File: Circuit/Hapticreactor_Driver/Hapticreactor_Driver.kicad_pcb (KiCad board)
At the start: 2 copper layers, 24 parts, among them IC1 XCL103D503CR-G, J1 Conn_01x02, J2 Conn_01x02, J3 Conn_01x02, U1 XIAO ESP32C3, U2 TB6552FNG_C_8_EL, U3 MCP4725xxx-xCH

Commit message: ハプティックリアクタ用基板完成
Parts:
- removed C2: 0.1u, Capacitor_SMD:C_0603_1608Metric_Pad1.08x0.95mm_HandSolder
- removed C3, C4: 10u, Capacitor_SMD:C_1206_3216Metric_Pad1.33x1.80mm_HandSolder
- removed IC1: XCL103D503CR-G, User:XCL103D503CRG
- removed R7: 10k, Resistor_SMD:R_0603_1608Metric_Pad0.98x0.95mm_HandSolder
- added H4: MountingHole, MountingHole:MountingHole_2.2mm_M2, F.Cu at (142.6, 70.4)
- C1, JP1, R1, R2, R3, R4, R5, U2, U3: moved to B.Cu
- C5: value C -> 0.1u; moved to B.Cu
- R6: value R -> 1k; moved to B.Cu
- moved R2 36.2 mm to (126.2, 72.3), turned to -90 degrees
- moved R1 36.2 mm to (124.6, 72.3), turned to 90 degrees
- moved J3 34.8 mm to (117.2, 77.0), turned to -90 degrees
- moved H1 32.7 mm to (116.4, 70.4)
- moved J2 32.5 mm to (141.6, 76.8), turned to 90 degrees
- moved H2 28.0 mm to (116.4, 84.4)
- moved C1 27.1 mm to (134.4, 71.0), turned to 90 degrees
- moved J1 24.4 mm to (141.6, 80.4), turned to 90 degrees
- moved U3 24.0 mm to (129.3, 83.1), turned to -90 degrees
- moved R3 23.1 mm to (133.2, 84.6)
- moved C5 22.6 mm to (132.5, 78.6)
- moved R6 20.6 mm to (125.6, 85.2)
- moved U2 19.8 mm to (130.4, 73.0), turned to 90 degrees
- moved H3 19.7 mm to (142.6, 84.4)
- moved JP1 18.3 mm to (132.6, 81.9), turned to 90 degrees
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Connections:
- R6 pad 1: /XIAO_ESP32_C3/D7/GPIO20 -> /XIAO_ESP32_C3/D6/GPIO6
- U2 pad 6: +5V -> +3.3V
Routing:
- net Net-(D1-A): track 0.00 -> 24.6 mm, vias 0 -> 1
- net /Motor_Driver/B_OUT_2: track 0.00 -> 20.4 mm
- net /Motor_Driver/B_OUT_1: track 0.00 -> 17.8 mm
- net +3.3V: track 0.00 -> 17.6 mm, vias 0 -> 3
- net /Motor_Driver/A_OUT_2: track 0.00 -> 17.4 mm, vias 0 -> 2
- net /DAC/DAC_OUT: track 0.00 -> 17.3 mm
- net /Motor_Driver/PWM_IN_B2: track 0.00 -> 17.3 mm, vias 0 -> 1
- net /Motor_Driver/A_OUT_1: track 0.00 -> 15.4 mm, vias 0 -> 2
- net /DAC/DAC_SDA: track 0.00 -> 14.9 mm, vias 0 -> 2
- net /Motor_Driver/PWM_IN_A2: track 0.00 -> 13.9 mm, vias 0 -> 1
- net /DAC/DAC_SCL: track 0.00 -> 13.7 mm, vias 0 -> 2
- net /XIAO_ESP32_C3/BATT_IN+: track 0.00 -> 13.6 mm
- net /Motor_Driver/PWM_IN_A1: track 0.00 -> 13.6 mm, vias 0 -> 1
- net /XIAO_ESP32_C3/BATT_IN-: track 0.00 -> 10.5 mm
- net /Motor_Driver/PWM_IN_B1: track 0.00 -> 9.48 mm, vias 0 -> 1
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- added copper zone on B.Cu, net +3.3V
- added copper zone on B.Cu, net GND
- added copper zone on F.Cu, net GND
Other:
- board outline added: 31 x 18.8 mm
- board text added: "A1 A2"
- board text added: "B1 B2"
- board text added: "D1/A1"
- board text added: "D2,D3"
- board text added: "D4"
- board text added: "D5"
- board text added: "D6"
- board text added: "D7,D10"
- board text added: "DAC"
- board text added: "I2C_Address 0x60 0x61"
- board text added: "Li-ion 3.7V"
- board text added: "Li-ion Vol"
- board text added: "PWM_A"
- board text added: "PWM_B"
- board text added: "SCL"
- board text added: "SDA"
- board text added: "→"

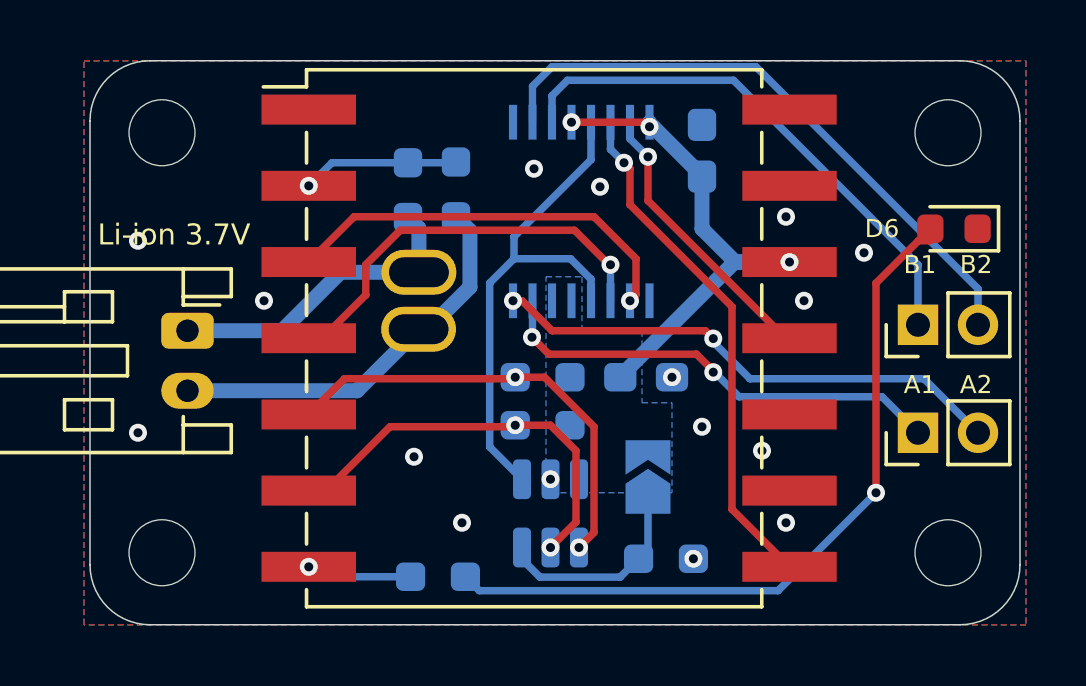
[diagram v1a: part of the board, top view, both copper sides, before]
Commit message: VMをバッテリ入力に変更，バッテリ周りの間違いを訂正
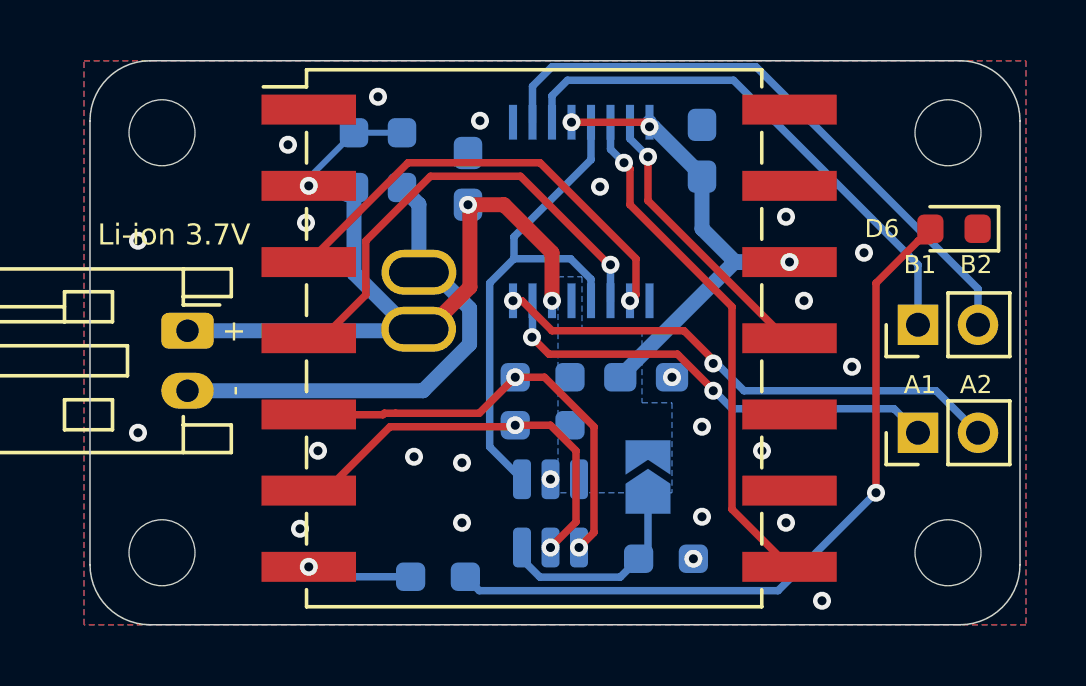
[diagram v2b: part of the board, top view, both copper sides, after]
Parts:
- added C2: 0.1u, Capacitor_SMD:C_0603_1608Metric_Pad1.08x0.95mm_HandSolder, B.Cu at (126.6, 71.9)
- moved R1 2.06 mm to (122.8, 71.3)
- moved R2 2.05 mm to (124.4, 71.3)
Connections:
- J3 pad 1: /XIAO_ESP32_C3/BATT_IN- -> +BATT
- J3 pad 2: /XIAO_ESP32_C3/BATT_IN+ -> /XIAO_ESP32_C3/BATT_IN-
- R1 pad 1: /XIAO_ESP32_C3/BATT_IN- -> +BATT
- R2 pad 2: /XIAO_ESP32_C3/BATT_IN+ -> /XIAO_ESP32_C3/BATT_IN-
- U1 pad B+: /XIAO_ESP32_C3/BATT_IN+ -> +BATT
- U2 pad 6: +3.3V -> +BATT
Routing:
- net +BATT: track 0.00 -> 23.6 mm, vias 0 -> 2
- net /XIAO_ESP32_C3/BATT_IN+: track 13.6 -> 0.00 mm
- net /XIAO_ESP32_C3/BATT_IN-: track 10.5 -> 16.7 mm
- net /Motor_Driver/PWM_IN_A2: track 13.9 -> 15.9 mm
- net /Motor_Driver/PWM_IN_A1: track 13.6 -> 15.1 mm
- net /XIAO_ESP32_C3/A1/ADC1: track 5.24 -> 3.99 mm
- net GND: track 0.00 -> 0.04 mm, vias 16 -> 24
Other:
- board text added: "+"
- board text added: "-"
- board text added: "I2C_Address 0x62 0x63"
- board text removed: "I2C_Address 0x60 0x61"
